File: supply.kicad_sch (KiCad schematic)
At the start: 102 parts, among them J12 1053131102, Q11 NX138BKMYL, Q12 NX138BKMYL, Q13 BCM857BS-7-F, Q14 BCM857BS-7-F, Q15 SSM3J332R, Q16 SSM3J332R, Q17 NX138BKMYL, Q18 SSM3J332R, Q19 NX138BKMYL, Q20 NX138BKMYL, Q21 NX138BKMYL, SW1 PCM12SMTR, U37 74LVC2G14GV, U38 74LVC1G175GV, U39 MP2386GG-P, U40 MP2386GG-P, U41 TPS7B8133DRVR, U42 TPS7A0518PDBVT

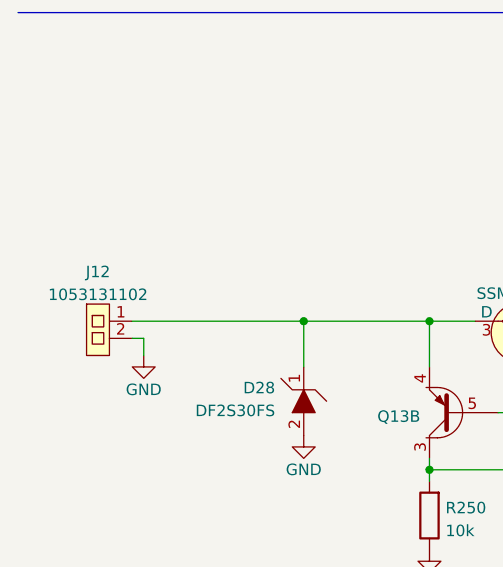
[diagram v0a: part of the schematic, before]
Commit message: Change power connector to SMD
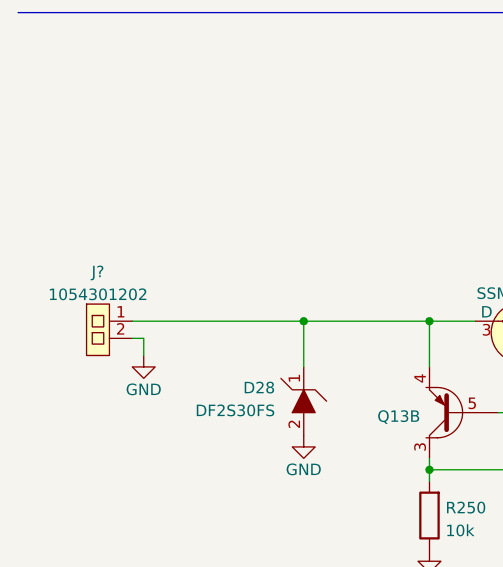
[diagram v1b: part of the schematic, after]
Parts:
- removed J12: 1053131102, antmicro-footprints:1053131102, symbol antmicroRectangularConnectorsHeadersFemalePins:1053131102
- added J?: Molex_Nano-Fit-105430_xx02-horizontal, antmicro-footprints:Molex_Nano-Fit_105430-xx02_1x02_P2.50mm_Horizontal_SMD, symbol antmicroRectangularConnectorsHeadersFemalePins:Molex_Nano-Fit-105430_xx02-horiz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
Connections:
- net GND: now also J?.2
- net at D28.1, Q13.4, Q15.3 (D): now also J?.1
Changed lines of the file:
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@@
     (pin "1")
+  )
+  (symbol (lib_id "antmicroRectangularConnectorsHeadersFemalePins:Molex_Nano-Fit-105430_xx02-horizontal") (at 20.32 127.635 0) (unit 1)
+    (in_bom yes) (on_board yes) (fields_autoplaced)
+    (property "Reference" "J?" (id 0) (at 21.59 124.0622 0))
+    (property "Value" "Molex_Nano-Fit-105430_xx02-horizontal" (id 1) (at 20.32 137.795 0)
+      (effects (font (size 1.27 1.27)) hide)
+    )
+    (property "Footprint" "antmicro-footprints:Molex_Nano-Fit_105430-xx02_1x02_P2.50mm_Horizontal_SMD" (id 2) (at 20.32 140.335 0)
+      (effects (font (size 1.27 1.27)) hide)
+    )
+    (property "Datasheet" "https://www.molex.com/pdm_docs/sd/1054301402_sd.pdf" (id 3) (at 20.32 142.875 0)
+      (effects (font (size 1.27 1.27)) hide)
+    )
+    (property "Manufacturer" "Molex" (id 4) (at 20.32 147.955 0)
+      (effects (font (size 1.27 1.27)) hide)
+    )
+    (property "MPN" "1054301202" (id 5) (at 20.32 145.415 0)
+      (effects (font (size 1.27 1.27)) hide)
+    )
+    (property "LICENSE" "MIT" (id 6) (at 20.32 150.495 0)
+      (effects (font (size 1.27 1.27)) hide)
+    )
+    (property "VAL" "1054301202" (id 7) (at 21.59 126.5991 0))
+    (pin "1")
+    (pin "2")
   )
   (symbol (lib_id "antmicroResistors0402:R_100k_0402") (at 248.92 251.46 90) (unit 1)
@@
     )
     (pin "1")
-    (pin "2")
-  )
-  (symbol (lib_id "antmicroRectangularConnectorsHeadersFemalePins:1053131102") (at 20.32 127.635 0) (unit 1)
-    (in_bom yes) (on_board yes) (fields_autoplaced)
-    (property "Reference" "J12" (id 0) (at 21.59 124.0622 0))
-    (property "Value" "1053131102" (id 1) (at 21.59 126.5991 0))
-    (property "Footprint" "antmicro-footprints:1053131102" (id 2) (at 15.875 135.89 0)
-      (effects (font (size 1.27 1.27)) hide)
-    )
-    (property "Datasheet" "" (id 3) (at 20.32 127.635 0)
-      (effects (font (size 1.27 1.27)) hide)
-    )
-    (property "Manufacturer" "Molex" (id 4) (at 19.05 140.97 0)
-      (effects (font (size 1.27 1.27)) hide)
-    )
-    (property "MPN" "1053131102" (id 5) (at 17.145 139.065 0)
-      (effects (font (size 1.27 1.27)) hide)
-    )
-    (pin "1")

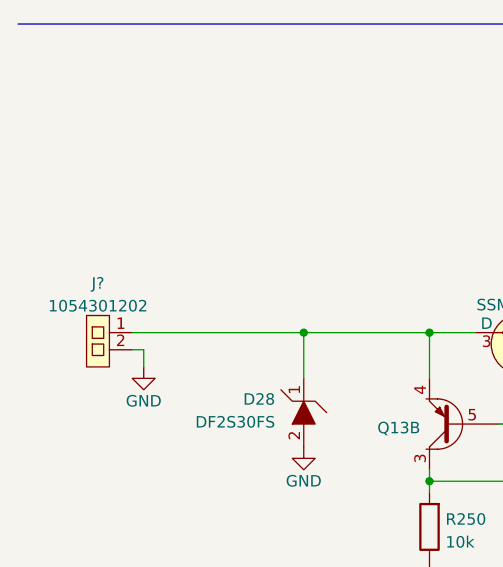
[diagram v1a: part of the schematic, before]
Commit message: Remove R0s from high speed signals, replace part of R0s with resistor ladder. Assign net clases
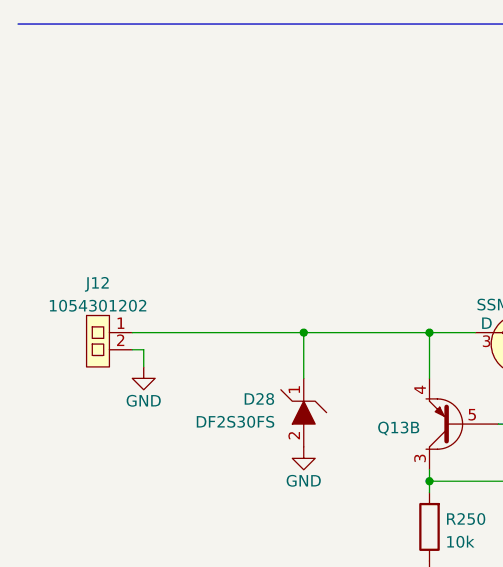
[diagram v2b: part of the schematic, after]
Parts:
- gave numbers to parts that had none: 1
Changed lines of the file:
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@@
   (symbol (lib_id "power:GND") (at 347.98 41.91 0) (unit 1)
     (in_bom yes) (on_board yes)
-    (property "Reference" "#PWR?" (id 0) (at 347.98 48.26 0)
+    (property "Reference" "#PWR0176" (id 0) (at 347.98 48.26 0)
       (effects (font (size 1.27 1.27)) hide)
     )
@@
   (symbol (lib_id "antmicroRectangularConnectorsHeadersFemalePins:Molex_Nano-Fit-105430_xx02-horizontal") (at 20.32 127.635 0) (unit 1)
     (in_bom yes) (on_board yes) (fields_autoplaced)
-    (property "Reference" "J?" (id 0) (at 21.59 124.0622 0))
+    (property "Reference" "J12" (id 0) (at 21.59 124.0622 0))
     (property "Value" "Molex_Nano-Fit-105430_xx02-horizontal" (id 1) (at 20.32 137.795 0)
       (effects (font (size 1.27 1.27)) hide)

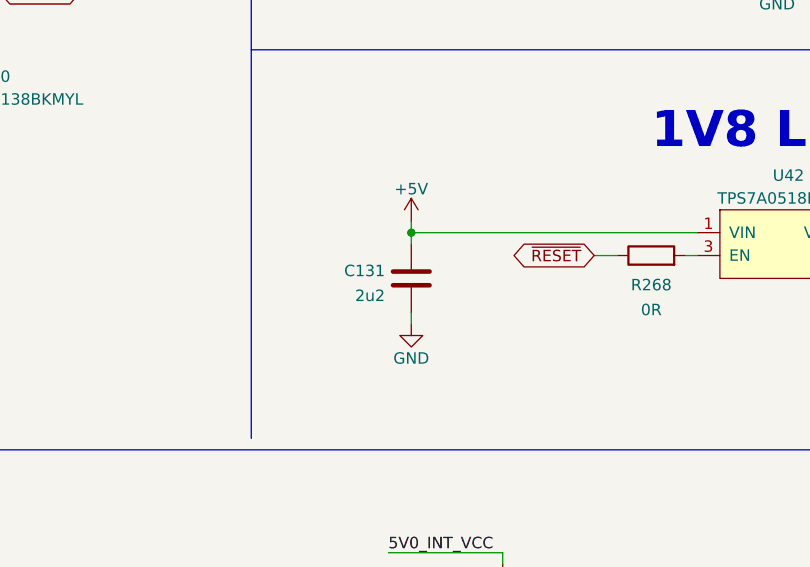
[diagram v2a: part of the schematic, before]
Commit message: Removed CSI mux LEDs and unified component types
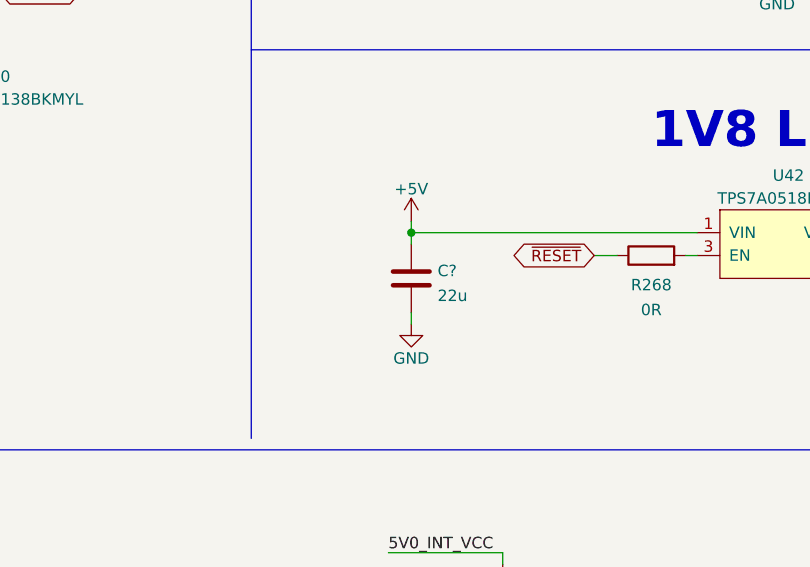
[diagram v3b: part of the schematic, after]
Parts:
- removed C131: C_2u2_0402, antmicro-footprints:0402-cap, symbol antmicroCapacitors0402:C_2u2_0402
- added C?: C_22u_0402, antmicro-footprints:0402-cap, symbol antmicroCapacitors0402:C_22u_0402
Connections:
- net +5V: now also C?.1
- net GND: now also C?.2
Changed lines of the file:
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@@
+    (pin "2")
+  )
+  (symbol (lib_id "antmicroCapacitors0402:C_22u_0402") (at 307.34 76.2 0) (unit 1)
+    (in_bom yes) (on_board yes) (fields_autoplaced)
+    (property "Reference" "C?" (id 0) (at 310.261 75.3654 0)
+      (effects (font (size 1.27 1.27)) (justify left))
+    )
+    (property "Value" "C_22u_0402" (id 1) (at 307.34 80.01 0)
+      (effects (font (size 1.27 1.27)) hide)
+    )
+    (property "Footprint" "antmicro-footprints:0402-cap" (id 2) (at 312.42 71.12 0)
+      (effects (font (size 1.524 1.524)) (justify left) hide)
+    )
+    (property "Datasheet" "" (id 3) (at 307.34 76.2 0)
+      (effects (font (size 1.27 1.27)) hide)
+    )
+    (property "Manufacturer" "AVX" (id 4) (at 312.42 66.04 0)
+      (effects (font (size 1.524 1.524)) (justify left) hide)
+    )
+    (property "MPN" "04024W226MAT2A" (id 5) (at 312.42 68.58 0)
+      (effects (font (size 1.524 1.524)) (justify left) hide)
+    )
+    (property "Val" "22u" (id 6) (at 310.261 78.1305 0)
+      (effects (font (size 1.27 1.27)) (justify left))
+    )
+    (pin "1")
     (pin "2")
   )
@@
     )
     (pin "1")
-    (pin "2")
-  )
-  (symbol (lib_id "antmicroCapacitors0402:C_2u2_0402") (at 307.34 76.2 0) (unit 1)
-    (in_bom yes) (on_board yes) (fields_autoplaced)
-    (property "Reference" "C131" (id 0) (at 304.4191 75.3654 0)
-      (effects (font (size 1.27 1.27)) (justify right))
-    )
-    (property "Value" "C_2u2_0402" (id 1) (at 307.34 80.01 0)
-      (effects (font (size 1.27 1.27)) hide)
-    )
-    (property "Footprint" "antmicro-footprints:0402-cap" (id 2) (at 312.42 71.12 0)
-      (effects (font (size 1.524 1.524)) (justify left) hide)
-    )
-    (property "Datasheet" "" (id 3) (at 307.34 76.2 0)
-      (effects (font (size 1.27 1.27)) hide)
-    )
-    (property "Manufacturer" "TDK" (id 4) (at 312.42 66.04 0)
-      (effects (font (size 1.524 1.524)) (justify left) hide)
-    )
-    (property "MPN" "C1005X5R1A225K050BC" (id 5) (at 312.42 68.58 0)
-      (effects (font (size 1.524 1.524)) (justify left) hide)
-    )
-    (property "Val" "2u2" (id 6) (at 304.4191 78.1305 0)
-      (effects (font (size 1.27 1.27)) (justify right))
-    )
-    (pin "1")

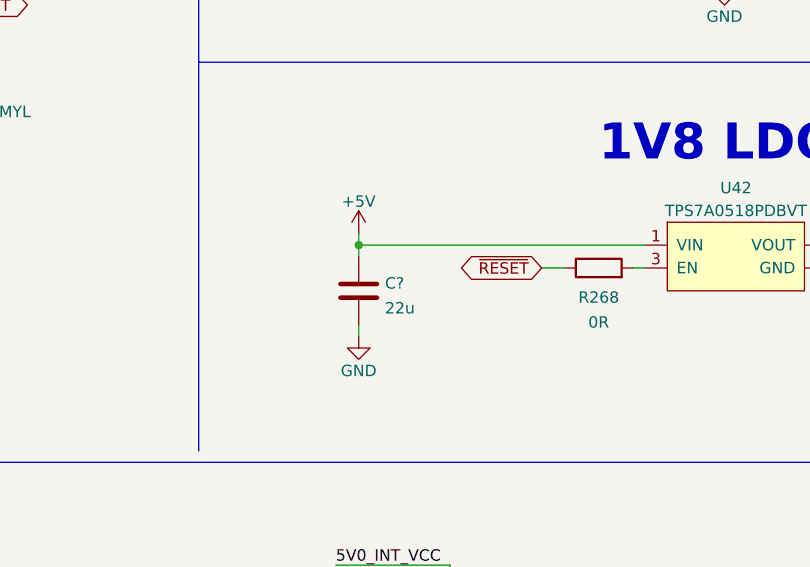
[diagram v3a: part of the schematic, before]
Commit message: Handled connection of unconnected pins and removed unnecessary labels
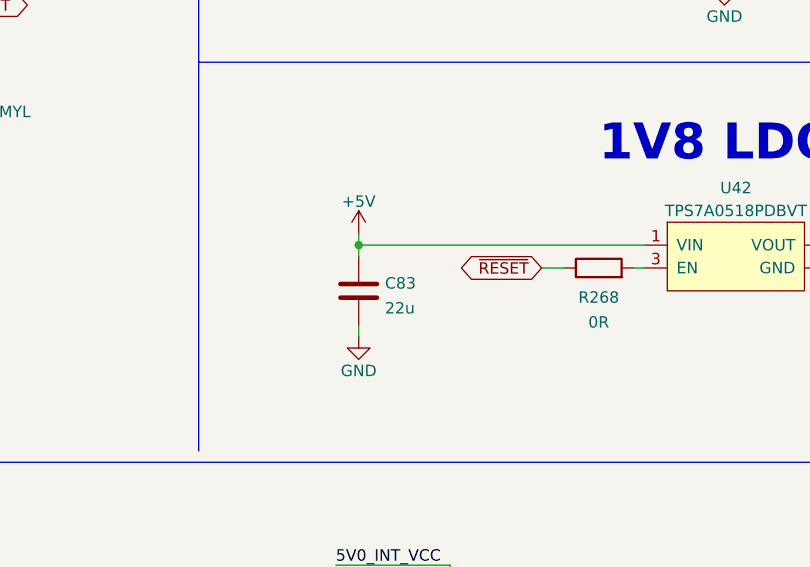
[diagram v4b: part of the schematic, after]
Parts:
- gave numbers to parts that had none: 1
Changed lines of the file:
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@@
   (symbol (lib_id "antmicroCapacitors0402:C_22u_0402") (at 307.34 76.2 0) (unit 1)
     (in_bom yes) (on_board yes) (fields_autoplaced)
-    (property "Reference" "C?" (id 0) (at 310.261 75.3654 0)
+    (property "Reference" "C83" (id 0) (at 310.261 75.3654 0)
       (effects (font (size 1.27 1.27)) (justify left))
     )

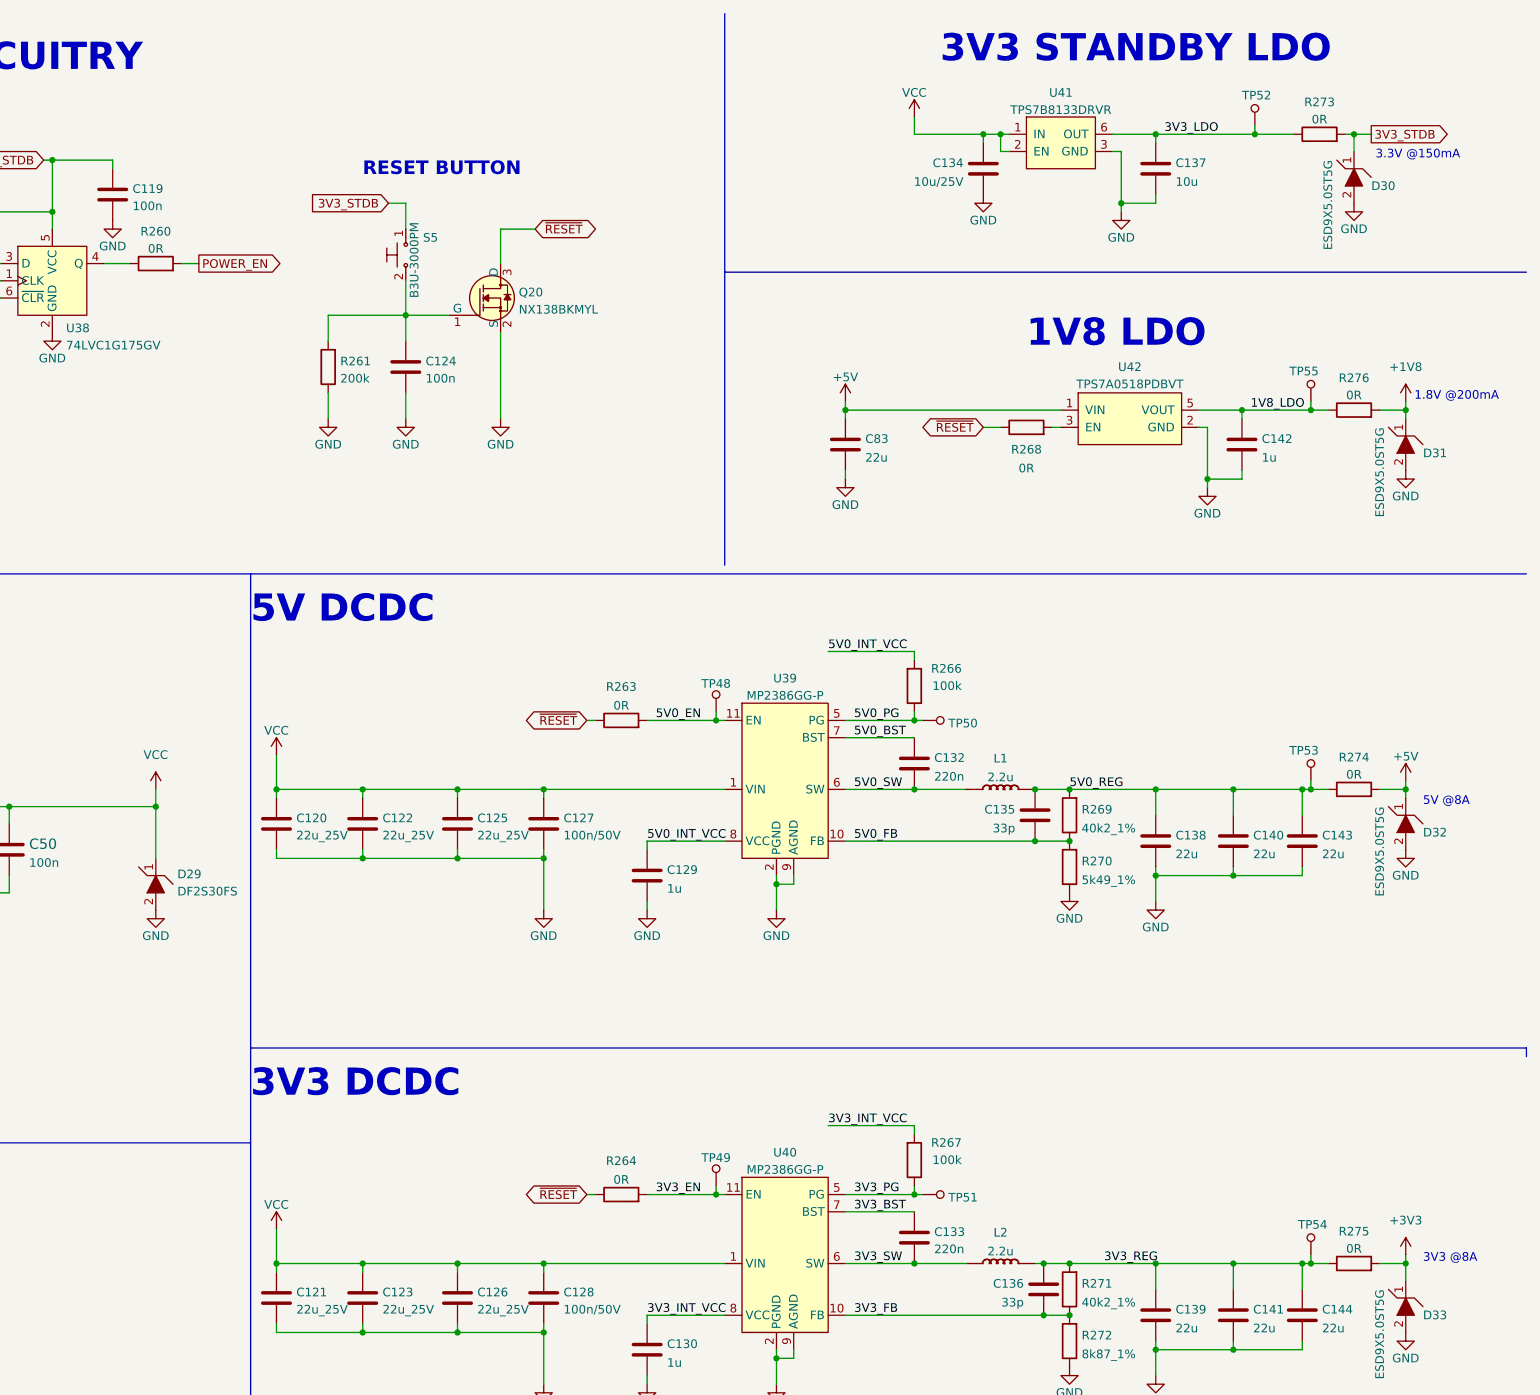
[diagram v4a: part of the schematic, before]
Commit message: Minor silkscreen/via/clearance cleanup
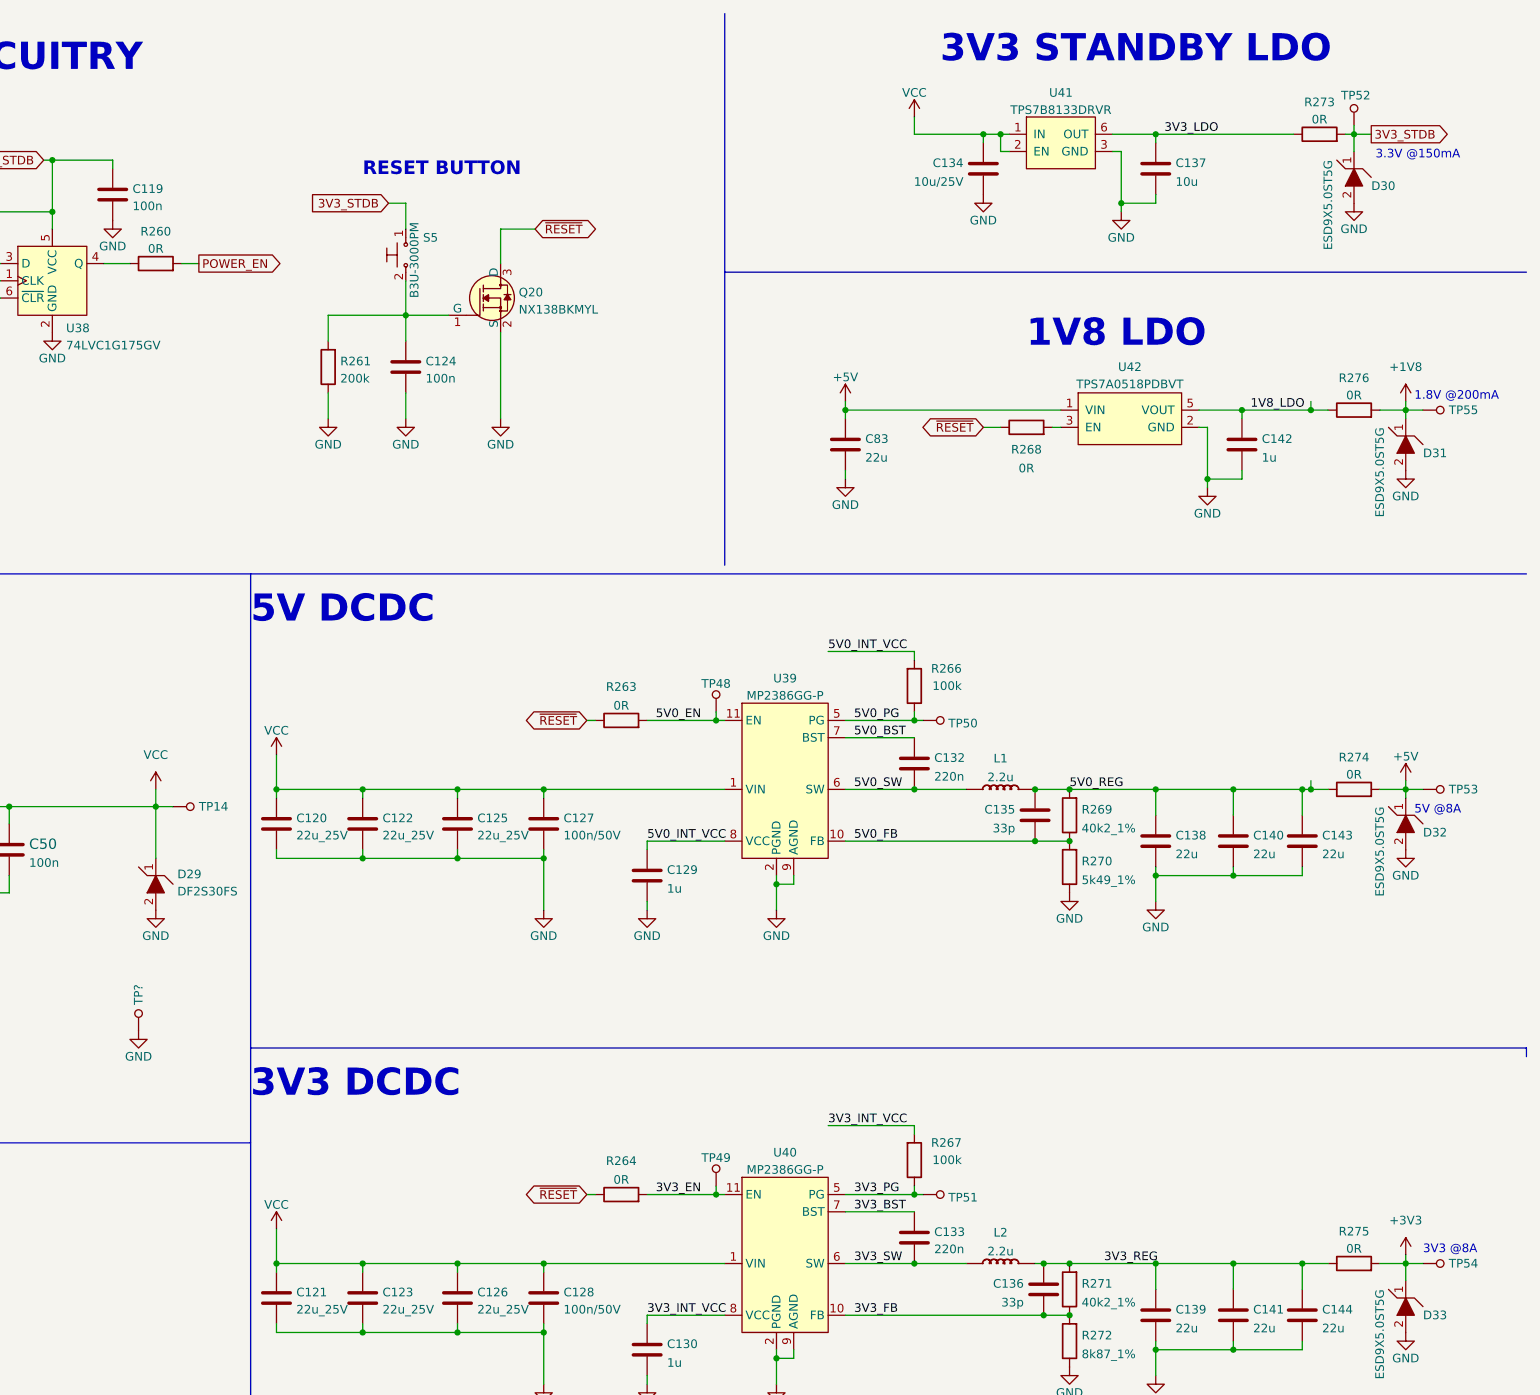
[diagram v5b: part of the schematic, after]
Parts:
- added TP14, TP?: TP_SMD_0_75MM, antmicro-footprints:Testpoint_smd_0_75mm, symbol antmicroTestPoints:TP_SMD_0_75MM
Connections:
- net +1V8: now also TP55.1
- net +3V3: now also TP54.1
- net +5V: now also TP53.1
- net 1V8_LDO: no longer TP55.1
- net 3V3_LDO: no longer TP52.1
- net 3V3_REG: no longer TP54.1
- net 3V3_STDB: now also TP52.1
- net 5V0_REG: no longer TP53.1
- net GND: now also TP?.1
- net VCC: now also TP14.1
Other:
- moved on the sheet: TP52, TP53, TP54, TP55
